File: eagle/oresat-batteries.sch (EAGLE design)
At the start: 313 parts, among them J1 J-SAMTEC-TFM-120-X1-XXX-D-RA, J4 ORESAT-DEBUG-CONNECTOR-ALL, Q1 DMP2240UDM, Q10 NTR4101, Q11 PMV45EN, Q12 Si7625DN, Q13 Si7625DN, Q14 NTR4101, Q15 NTR4101, Q16 Si7625DN, Q17 Si7625DN, Q18 Si7625DN, Q19 Si7625DN, Q2 PMV45EN, Q20 Si7625DN, Q21 PMV45EN, Q22 PMV45EN, Q23 NTR4101, Q24 PM45VEN, Q25 PM45VEN, Q26 PM45VEN, Q27 PM45VEN, Q28 NTR4101, Q29 PM45VEN, Q3 DMP3050LVT-7, Q30 Si7625DN, Q31 Si7625DN, Q32 NTR4101, Q33 NTR4101, Q34 Si7625DN, Q35 Si7625DN, Q36 Si7625DN, Q37 Si7625DN, Q38 Si7625DN, Q39 PM45VEN, Q4 DMP3050LVT-7, Q40 PM45VEN, Q41 NTR4101, Q42 DMP2240UDM, Q43 DMP2240UDM, Q5 PMV45EN, Q6 PM45VEN, Q7 PM45VEN, Q8 PM45VEN, Q9 PM45VEN, U1 MAX7310ATE, U10 LTC4412, U11 LTC4412, U12 MAX17205G, U13 S-8209AAA-T8T1U, U14 S-8209AAA-T8T1U, U15 LTC4412, U16 LTC4412, U17 MAX17205G, U2 MIC842LYC5, U20 TCAN330, U21 STM32F091C, U3 MIC842LYC5, U4 MAX4211FETE, U5 TPS62111RSA, U8 S-8209AAA-T8T1U, U9 S-8209AAA-T8T1U, X3 16MHZ-2.5x2mm

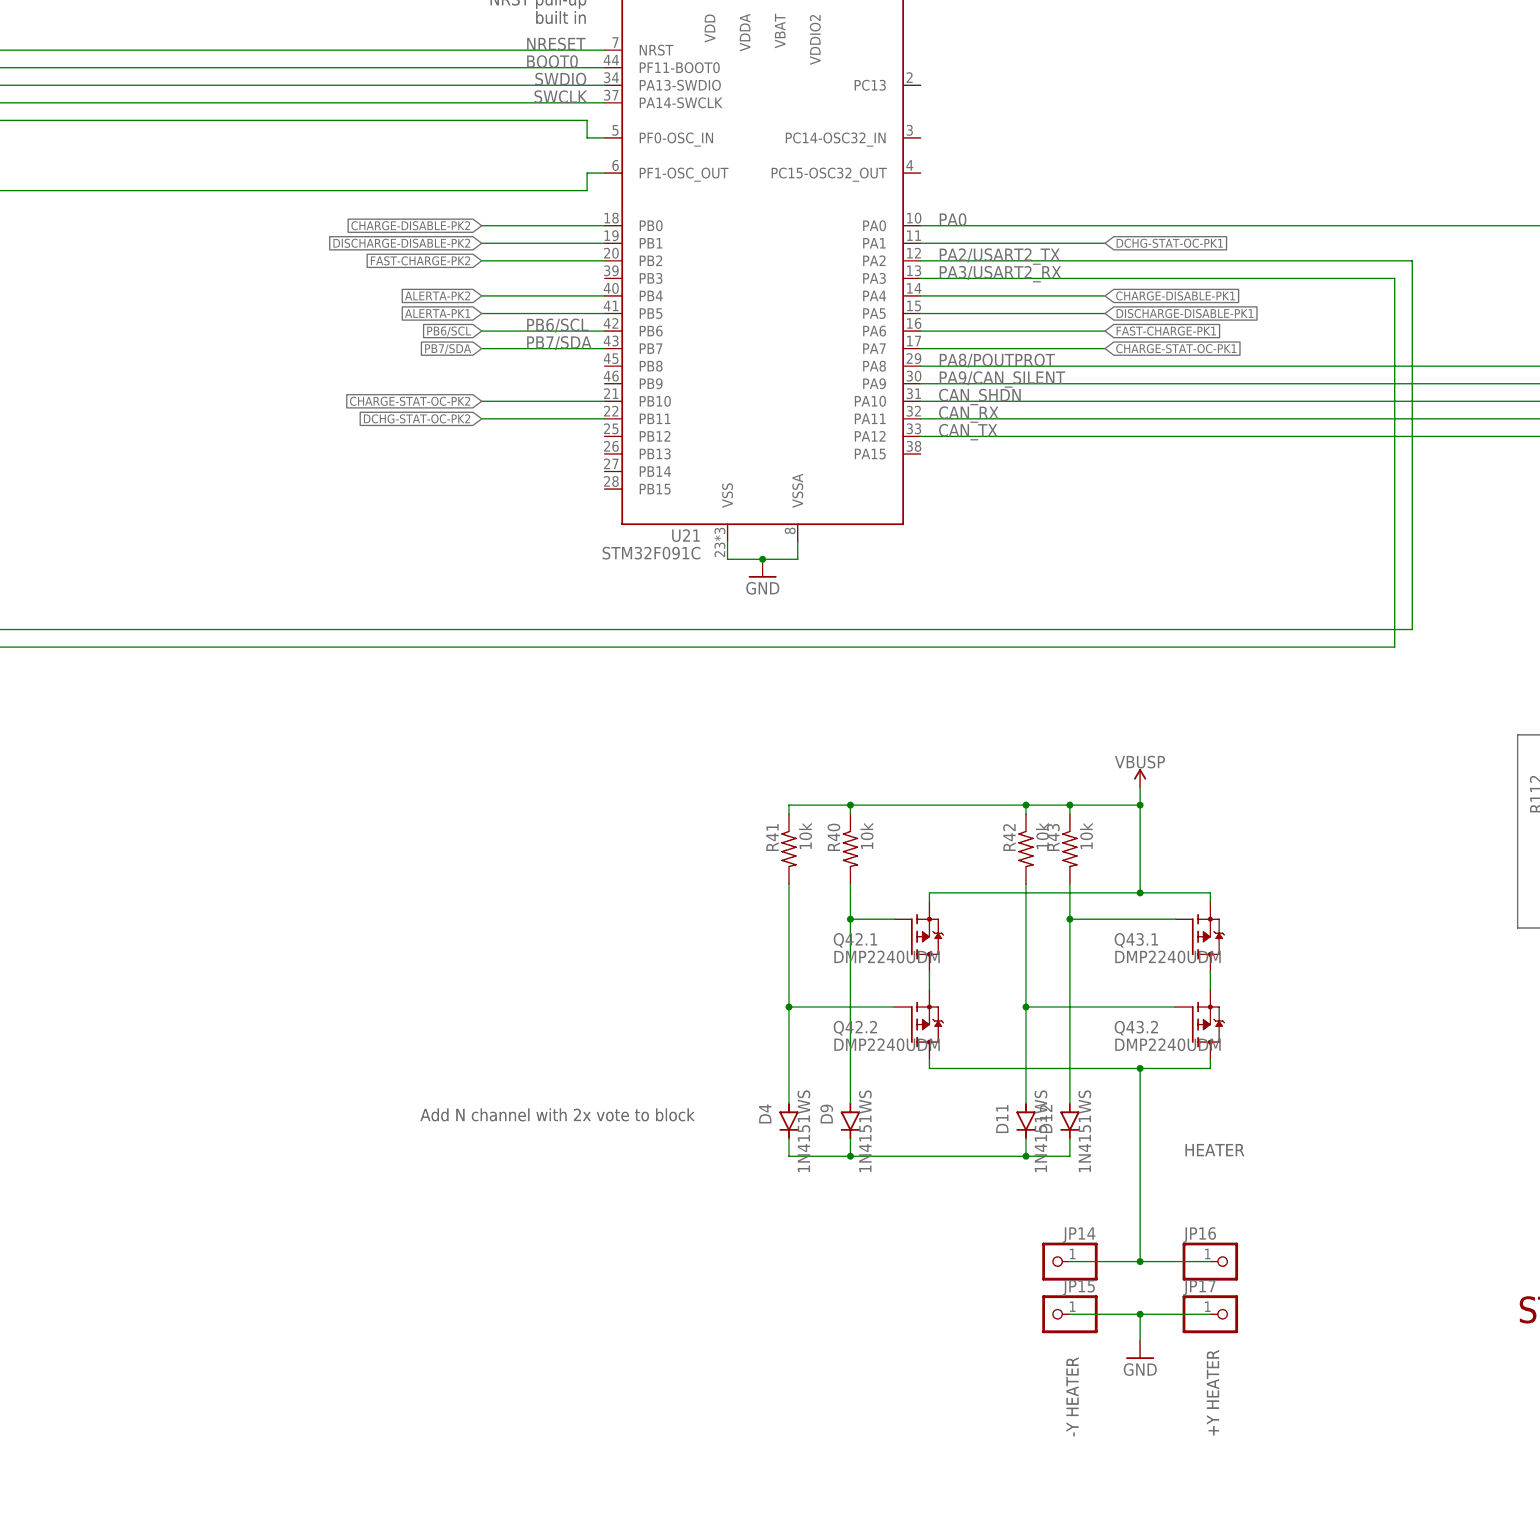
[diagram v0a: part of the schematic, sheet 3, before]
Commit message: Updated README, killed design documents. Also, finished layout. Still need to polish, but heater is layed out and doesn't seem to be terrible.
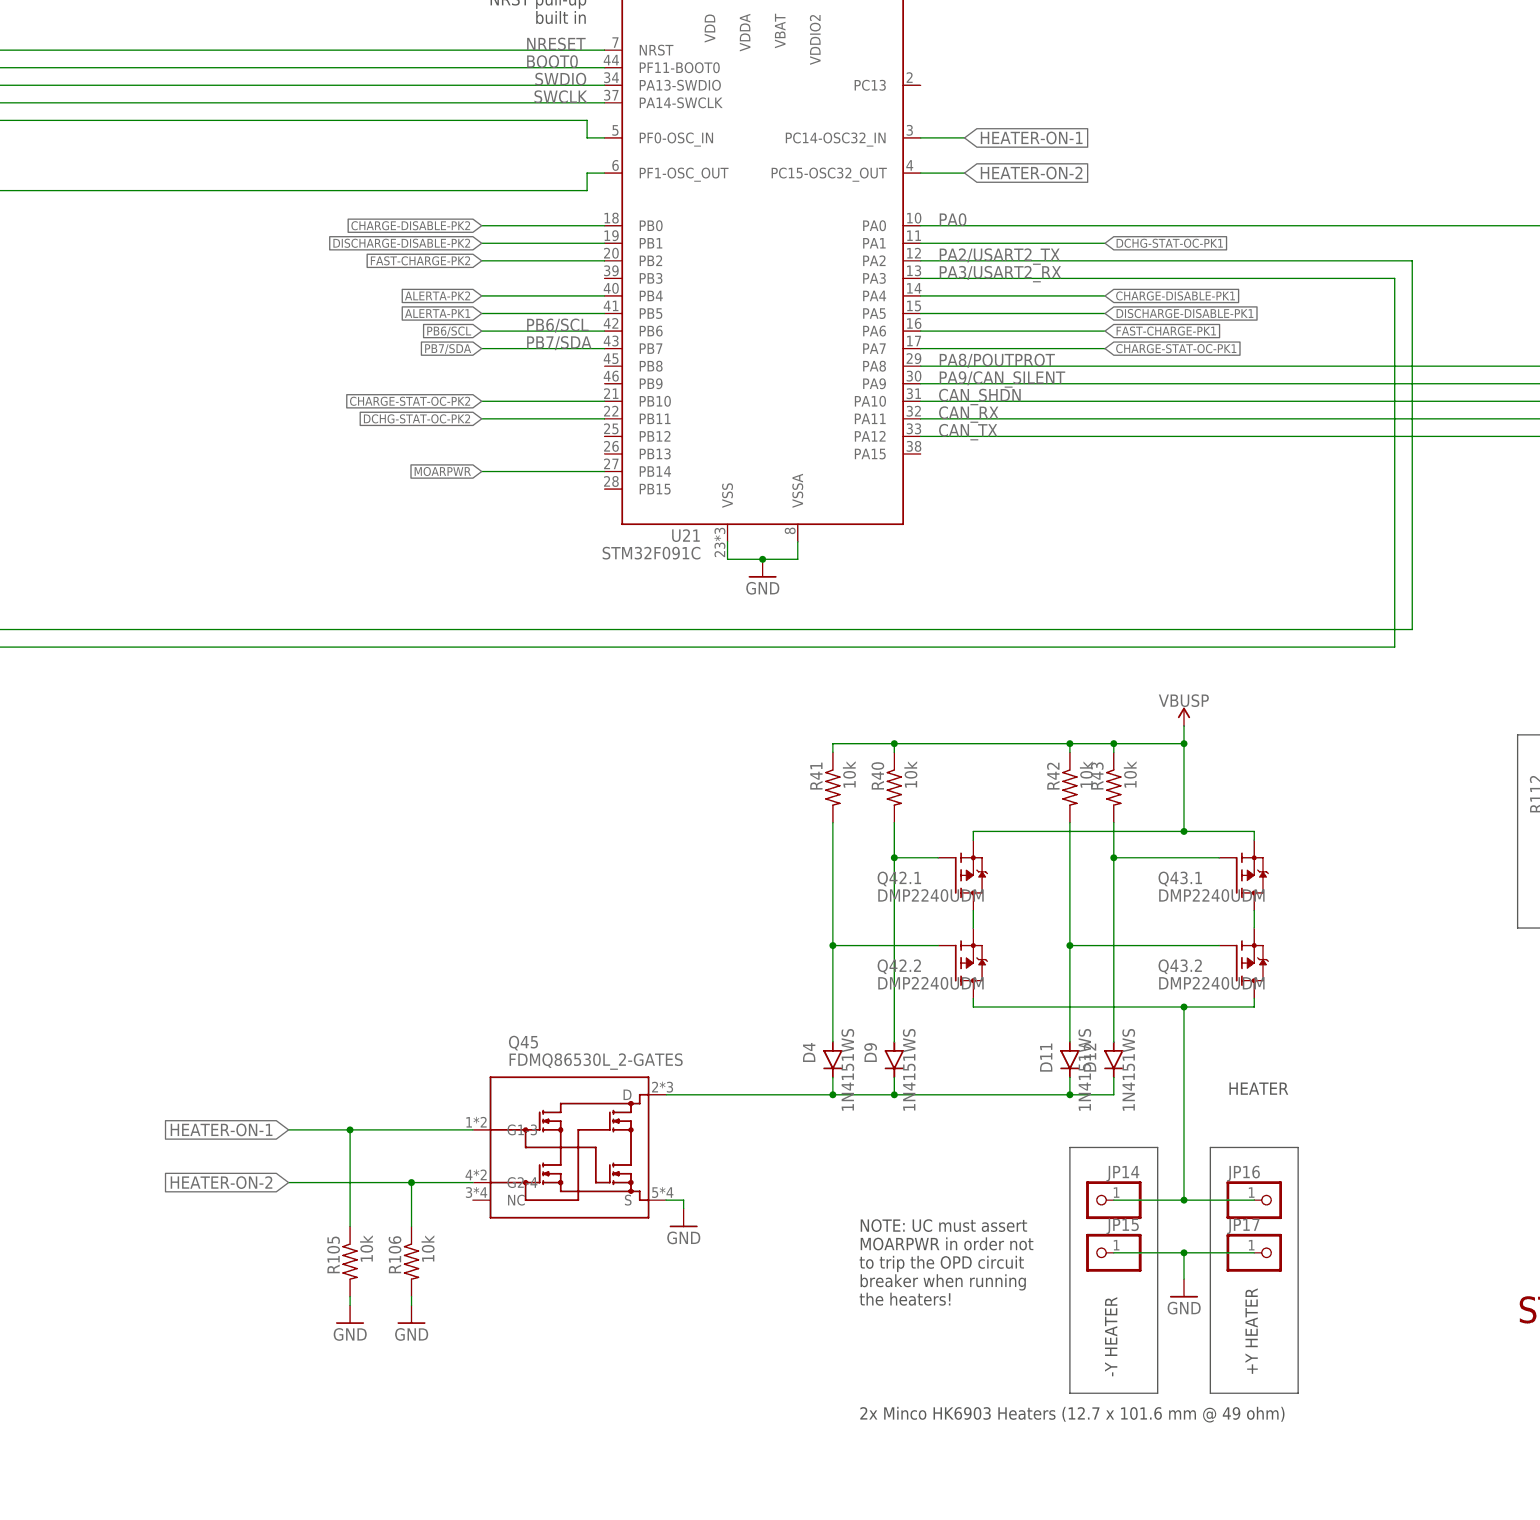
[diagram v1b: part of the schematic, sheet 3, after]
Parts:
- added Q44: PMV45EN, Q-MOSFET-NCH-SOT23-3:N-MOSFET-SOT-23-3
- added Q45: FDMQ86530L_2-GATES, Q-On_Semiconductor-FDMQ86530L-MOSFET-4-N-CH:FDMQ86530L_2-GATES
- added R105, R106, R44: 10k, oresat-rcl:R-US_0603-C-NOSILK
- R32: value 0 -> 10k
- R34: value NP -> 20k
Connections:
- net N$92 renamed HEATER
- new net HEATER-ON-1: Q45.G1-3, R105.1, U21.PC14-OSC32_IN
- new net HEATER-ON-2: Q45.G2-4, R106.1, U21.PC15-OSC32_OUT
- new net MOARPWR: Q44.G, R44.2, U21.PB14
- new net N$29: Q44.D, R34.1
- net GND: now also Q44.S, Q45.S, R105.2, R106.2, R44.1; no longer R34.1
- net N$64: now also Q45.D
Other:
- note added: "2x Minco HK6903 Heaters (12.7 x 101.6 mm @ 49 ohm)"
- note added: "Increase CB limit from 300 mA to 375 mA"
- note added: "NOTE: UC must assert MOARPWR in order not to trip the OPD circuit breaker when running the heaters!"
- note removed: "Add N channel with 2x vote to block"
- note removed: "If it's really vbusp, we need to increase the current in the CB"
- moved on the sheet: D11, D12, D4, D9, JP14, JP15, JP16, JP17, Q42.1, Q42.2, Q43.1, Q43.2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

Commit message: Polished battery board.
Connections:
- net N$54 renamed INTERCELL-PK1
- net N$88 renamed INTERCELL-PK2
- net VBATT-PK1 renamed VBATT-POS-PK1
- net VBATT-PK2 renamed VBATT-POS-PK2
- removed net N$1: JP6.1, R62.1, U12.CSP
- removed net N$13: JP12.1, R92.1, U17.CSP
- new net VBATT-NEG-PK1: B2.NEG, C15.2, C16.2, C21.2, JP5.1, Q6.S, Q7.S, Q8.S, Q9.S, R47.1, R50.1, R61.2, TP42.1, U8.VSS
- new net VBATT-NEG-PK2: B4.NEG, C26.2, C27.2, C32.2, JP7.1, Q24.S, Q25.S, Q26.S, Q27.S, R77.1, R80.1, R91.2, TP65.1, U13.VSS
- net CSP-PK1: now also JP6.1, R62.1, U12.CSP; no longer B2.NEG, C15.2, C16.2, C21.2, JP5.1, Q6.S, Q7.S, Q8.S, Q9.S, R47.1, R50.1, R61.2, TP42.1, U8.VSS
- net CSP-PK2: now also JP12.1, R92.1, U17.CSP; no longer B4.NEG, C26.2, C27.2, C32.2, JP7.1, Q24.S, Q25.S, Q26.S, Q27.S, R77.1, R80.1, R91.2, TP65.1, U13.VSS
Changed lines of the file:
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@@
 </segment>
 </net>
-<net name="VBUS" class="0">
+<net name="VBUS" class="2">
 <segment>
 <label x="168.91" y="152.4" size="2.54" layer="95" xref="yes"/>
@@
 </segment>
 </net>
-<net name="VBUS" class="0">
+<net name="VBUS" class="2">
 <segment>
 <pinref part="VBUS1" gate="1" pin="VBUS"/>
@@
 <pinref part="TP66" gate="G$1" pin="1"/>
 <junction x="256.54" y="41.91"/>
+<label x="281.94" y="45.72" size="1.778" layer="95"/>
 </segment>
 <segment>
@@
 </segment>
 </net>
-<net name="VBATT-PK2" class="0">
+<net name="VBATT-POS-PK2" class="2">
 <segment>
 <wire x1="256.54" y1="148.59" x2="256.54" y2="160.02" width="0.508" layer="91"/>
@@
 <wire x1="148.59" y1="173.99" x2="213.36" y2="173.99" width="0.1524" layer="91"/>
 <junction x="256.54" y="148.59"/>
-<label x="257.81" y="151.13" size="1.778" layer="95"/>
+<label x="264.16" y="148.59" size="1.778" layer="95"/>
 <junction x="148.59" y="173.99"/>
 <pinref part="R84" gate="R" pin="2"/>
@@
 <junction x="256.54" y="135.89"/>
 <pinref part="F2" gate="G$1" pin="P$2"/>
+<label x="184.15" y="173.99" size="1.778" layer="95"/>
 </segment>
 </net>
@@
 </segment>
 </net>
-<net name="VBUS" class="0">
+<net name="VBUS" class="2">
 <segment>
 <pinref part="VBUS4" gate="1" pin="VBUS"/>
@@
 </segment>
 </net>
-<net name="VBATT-F-PK2" class="0">
+<net name="VBATT-F-PK2" class="2">
 <segment>
 <wire x1="237.49" y1="209.55" x2="237.49" y2="207.01" width="0.508" layer="91"/>
@@
 </segment>
 </net>
-<net name="CSP-PK2" class="2">
+<net name="VBATT-NEG-PK2" class="2">
 <segment>
 <pinref part="R91" gate="R" pin="2"/>
@@
 <pinref part="B4" gate="G$1" pin="NEG"/>
 <pinref part="JP7" gate="G$1" pin="1"/>
+<label x="184.15" y="76.2" size="1.778" layer="95"/>
+<label x="30.48" y="53.34" size="1.778" layer="95" rot="R90"/>
 </segment>
 </net>
@@
 </segment>
 </net>
-<net name="N$88" class="2">
+<net name="INTERCELL-PK2" class="2">
 <segment>
 <pinref part="C26" gate="CE" pin="1"/>
@@
 <pinref part="TP63" gate="G$1" pin="1"/>
 <pinref part="B3" gate="G$1" pin="NEG"/>
+<label x="184.15" y="110.49" size="1.778" layer="95"/>
+<label x="30.48" y="111.76" size="1.778" layer="95" rot="R90"/>
 </segment>
 </net>
-<net name="N$89" class="0">
+<net name="N$89" class="2">
 <segment>
 <wire x1="275.59" y1="215.9" x2="275.59" y2="210.82" width="0.508" layer="91"/>
@@
 </segment>
 </net>
-<net name="N$13" class="0">
+<net name="CSP-PK2" class="2">
 <segment>
 <pinref part="U17" gate="A" pin="CSP"/>
@@
 <wire x1="256.54" y1="55.88" x2="336.55" y2="55.88" width="0.1524" layer="91"/>
 <junction x="256.54" y="55.88"/>
+<label x="281.94" y="55.88" size="1.778" layer="95"/>
 </segment>
 </net>
@@
 <wire x1="256.54" y1="38.1" x2="256.54" y2="35.56" width="0.508" layer="91"/>
 <junction x="256.54" y="38.1"/>
+<label x="279.4" y="41.91" size="1.778" layer="95"/>
 </segment>
 </net>
@@
 </segment>
 </net>
-<net name="VBATT-PK1" class="0">
+<net name="VBATT-POS-PK1" class="2">
 <segment>
 <wire x1="256.54" y1="148.59" x2="256.54" y2="160.02" width="0.508" layer="91"/>
@@
 <junction x="256.54" y="135.89"/>
 <pinref part="F1" gate="G$1" pin="P$2"/>
+<label x="181.61" y="173.99" size="1.778" layer="95"/>
 </segment>
 </net>
@@
 </segment>
 </net>
-<net name="VBUS" class="0">
+<net name="VBUS" class="2">
 <segment>
 <pinref part="VBUS3" gate="1" pin="VBUS"/>
@@
 </segment>
 </net>
-<net name="VBATT-F-PK1" class="0">
+<net name="VBATT-F-PK1" class="2">
 <segment>
 <wire x1="237.49" y1="209.55" x2="237.49" y2="207.01" width="0.508" layer="91"/>
@@
 </segment>
 </net>
-<net name="CSP-PK1" class="2">
+<net name="VBATT-NEG-PK1" class="2">
 <segment>
 <pinref part="R61" gate="R" pin="2"/>
@@
 <junction x="256.54" y="73.66"/>
 <pinref part="JP5" gate="G$1" pin="1"/>
+<label x="182.88" y="76.2" size="1.778" layer="95"/>
 </segment>
 </net>
@@
 </segment>
 </net>
-<net name="N$54" class="2">
+<net name="INTERCELL-PK1" class="2">
 <segment>
 <pinref part="C15" gate="CE" pin="1"/>
@@
 <junction x="45.72" y="130.81"/>
 <pinref part="TP40" gate="G$1" pin="1"/>
+<label x="182.88" y="110.49" size="1.778" layer="95"/>
 </segment>
 </net>
-<net name="N$41" class="0">
+<net name="N$41" class="2">
 <segment>
 <wire x1="275.59" y1="215.9" x2="275.59" y2="210.82" width="0.508" layer="91"/>
@@
 </segment>
 </net>
-<net name="N$1" class="2">
+<net name="CSP-PK1" class="2">
 <segment>
 <pinref part="U12" gate="A" pin="CSP"/>
@@
 <junction x="256.54" y="52.07"/>
 <pinref part="JP6" gate="G$1" pin="1"/>
+<label x="279.4" y="52.07" size="1.778" layer="95"/>
 </segment>
 </net>

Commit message: fixed a couple left over attributes and formatted BOM
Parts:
- B1, B2, B3, B4: DIS (none) -> Tenergy; DPN (none) -> MH48285; MFR (none) -> Tenergy; MPN (none) -> MH48285
- C1, C2, C4: DPN 311-1446-1-ND -> 1276-6524-1-ND; MFR Yageo -> Samsung; MPN CC0603KRX7R7BB105 -> CL10B105MO8NNWC
- C15, C17, C19, C22, C23, C26, C28, C30, C33, C34: DIS (none) -> Digi-Key; DPN (none) -> 399-1099-1-ND; MFR (none) -> Kemet; MPN (none) -> C0603C104M4RACTU
- C16, C18: DIS (none) -> Digi-Key; DPN (none) -> 399-7842-1-ND; MFR (none) -> Kemet; MPN (none) -> C0603C103M5RACTU
- C20, C21, C31, C32: DIS (none) -> Digi-Key; DPN (none) -> 311-1080-1-ND; MFR (none) -> Yageo; MPN (none) -> CC0603KRX7R9BB102
- C24, C25, C35, C36: DIS (none) -> Digi-Key; DPN (none) -> 399-7934-1-ND; MFR (none) -> Kemet; MPN (none) -> C0603C474K4PACTU
- C27, C29: DPN (none) -> 399-7842-1-ND; MFR (none) -> Kemet; MPN (none) -> C0603C103M5RACTU
- C3: DPN 1276-1001-1-ND -> 399-1099-1-ND
- C44, C45, C48, C49, C50: DPN 1276-1001-1-ND -> 399-1099-1-ND; MPN CL05B104KO5NNNC -> C0603C104M4RACTU
- C46, C47: DPN 1276-6601-1-ND -> 311-1424-1-ND; MFR Samsung -> Yageo; MPN CL05C200JB51PNC -> CC0603JRNPO9BN200
- C5: DPN 1276-6472-1-ND -> 1276-2893-1-ND; MPN CL21B106KOQNNNG -> CL21A106KOFNNNE
- C8: DPN 490-9959-1-ND -> 490-10511-1-ND; MPN GRM21BD71A226ME44L -> GRM21BR61A226ME51L
- D11, D12, D4, D5, D6, D7, D8, D9: DIS (none) -> Digi-Key; DPN (none) -> 112-1N4151WS-E3-08CT-ND; MFR (none) -> Vishay; MPN (none) -> 1N4151WS-E3-08
- F1, F2: DIS (none) -> Digi-Key; DPN (none) -> F9966CT-ND; MFR (none) -> LittleFuse; MPN (none) -> NANOSMD350LR-C-2
- J4: DIS (none) -> Digi-Key; DPN (none) -> A100287CT-ND; MFR (none) -> TE; MPN (none) -> 2-1734592-0
- Q1: DPN DMP2240UDMDICT-ND -> GRM21BR61A226ME51L
- Q10, Q23: DIS (none) -> Digi-Key; DPN (none) -> NTR4101PT1GOSCT-ND; MFR (none) -> On Semi; MPN (none) -> NTR4101PT1G
- Q11, Q21, Q22, Q24, Q25, Q26, Q27, Q29, Q39, Q40, Q6, Q7, Q8, Q9: DIS (none) -> Digi-Key; DPN (none) -> 1727-2307-1-ND; MFR (none) -> Nexperia; MPN (none) -> PMV45EN2R
- Q12, Q13, Q16, Q17, Q18, Q19, Q20, Q30, Q31, Q34, Q35, Q36, Q37, Q38: DIS (none) -> Digi-Key; DPN (none) -> SI7625DN-T1-GE3CT-ND; MFR (none) -> Vishay; MPN (none) -> SI7625DN-T1-GE3
- Q14, Q15, Q28, Q32, Q33, Q41: DIS (none) -> Digi-Key; DPN (none) -> NTR4101PT1GOSCT-ND; MFR (none) -> ON Semi; MPN (none) -> NTR4101PT1G
- Q45: DPN (none) -> FDMQ86530LCT-ND; MFR (none) -> ON Semi; MPN (none) -> FDMQ86530L
- R1: DPN 311-100LRCT-ND -> 311-10.0HRCT-ND; MPN RC0402FR-07100RL -> RC0603FR-0710RL
- R10, R11, R14, R15, R16, R17, R2, R3, R4, R5, R8, R9: DPN 1276-4275-1-ND -> 311-665KHRCT-ND; MFR Samsung -> Yageo; MPN RC1005F6653CS -> RC0603FR-07665KL
- R100, R102, R103, R104, R47, R50, R55, R56, R69, R70, R72, R73, R74, R77, R80, R85, R86, R99: DIS (none) -> Digi-Key; DPN (none) -> 311-10.0KHRCT-ND; MFR (none) -> Yageo; MPN (none) -> RC0603FR-0710KL
- R101, R71: DIS (none) -> Digi-Key; DPN RNCP0603FTD10K0CT-ND -> 311-10.0KHRCT-ND; MFR (none) -> Yageo; MPN RNCP0603FTD10K0 -> RC0603FR-0710KL
- R105, R106, R110, R112, R18, R24, R25, R28, R31, R37, R38, R40, R41, R42, R43, R44: DPN 311-10.0KLRCT-ND -> 311-10.0KHRCT-ND; MPN RC0402FR-0710KL -> RC0603FR-0710KL
- R111, R23, R36, R39: DPN A129632CT-ND -> A129693CT-ND; MFR TE Connectivity -> TE; MPN CRGCQ0402F2K7 -> CRGCQ0603F2K7
- R113, R114: DPN A129632CT-ND -> RR08P4.7KDCT-ND; MPN CRGCQ0402F2K7 -> RR0816P-472-D
- R12, R13: DPN 311-10.0KLRCT-ND -> 311-665KHRCT-ND; MPN RC0402FR-0710KL -> RC0603FR-07665KL
- R19, R20: DPN 749-1575-1-ND -> A129718CT-ND; MFR Vishay -> TE; MPN MCS04020C3303FE000 -> CRGCQ0603F330K
- R21, R22: DPN 311-1.00MLRCT-ND -> 311-1.00MHRCT-ND; MPN RC0402FR-071ML -> RC0603FR-071ML
- R32: DPN 311-0.0JRCT-ND -> 311-10.0KHRCT-ND; MPN RC0402JR-070RL -> RC0603FR-0710KL
- R33: DPN 311-0.0JRCT-ND -> 311-0.0GRCT-ND; MPN RC0402JR-070RL -> RC0603JR-070RL
- R34: DPN 1276-4275-1-ND -> RR08P20.0KDCT-ND; MPN RC1005F6653CS -> RR0816P-203-D
- R45, R48, R52, R53: DIS (none) -> Yageo; DPN (none) -> RC0603JR-071KL; MPN (none) -> 311-1.0KGRCT-ND
- R46, R49, R58, R59, R60, R61, R76, R79, R88, R89, R90, R91: DIS (none) -> Digi-Key; DPN (none) -> 311-1.00MHRCT-ND; MFR (none) -> Yageo; MPN (none) -> RC0603FR-071ML
- R51, R54, R81, R84: DIS (none) -> Digi-Key; DPN (none) -> 311-470GRCT-ND; MFR (none) -> Yageo; MPN (none) -> RC0603JR-07470RL
- R57, R64, R67, R68: DIS (none) -> Digi-Key; DPN (none) -> RR08P100KDCT-ND; MFR (none) -> Susumu; MPN (none) -> RR0816P-104-D
- R6, R7: DPN 311-100LRCT-ND -> 311-100HRCT-ND; MPN RC0402FR-07100RL -> RC0603FR-07100RL
- R62, R92: DIS (none) -> Digi-Key; DPN (none) -> 696-1374-1-ND; MFR (none) -> Riedon; MPN (none) -> CSR1206-0R01F1
- R63, R93: DIS (none) -> Digi-Key; DPN (none) -> 311-100FRCT-ND; MFR (none) -> Yageo; MPN (none) -> RC1206FR-07100RL
- R65, R95: DIS (none) -> Digi-Key; DPN (none) -> 311-10.0HRCT-ND; MFR (none) -> Yageo; MPN (none) -> RC0603FR-0710RL
- R66, R96: DIS (none) -> Digi-Key; DPN (none) -> 311-100HRCT-ND; MFR (none) -> Yageo; MPN (none) -> RC0603FR-07100RL
- R75, R78, R82, R83: DIS (none) -> Digi-Key; DPN (none) -> 311-1.0KGRCT-ND; MFR (none) -> Yageo; MPN (none) -> RC0603JR-071KL
- R87, R94, R97, R98: DIS (none) -> Digi-Key; DPN (none) -> RR08P100KDCT-ND; MFR (none) -> Yageo; MPN (none) -> RR0816P-104-D
- U10, U11, U15, U16: DIS (none) -> Digi-Key; DPN (none) -> LTC4412ES6#TRPBFCT-ND; MFR (none) -> Analog Devices; MPN (none) -> LTC4412ES6#TRPBF
- U12: DIS (none) -> Distributor; DPN (none) -> MAX17205G+TCT-ND; MFR (none) -> Maxim; MPN (none) -> MAX17205G+T
- U17: DIS (none) -> Digi-Key; DPN (none) -> MAX17205G+TCT-ND; MFR (none) -> Maxim; MPN (none) -> MAX17205G+T
- U2: DIS (none) -> Digi-Key; DPN (none) -> 576-2927-1-ND; MFR (none) -> Microchip; MPN (none) -> MIC842LYC5-TR
- U21: DPN 497-18516-ND -> 497-17364-ND; MPN STM32F042K6T7 -> STM32F091CBT6
